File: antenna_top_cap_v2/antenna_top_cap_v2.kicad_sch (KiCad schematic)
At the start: 55 parts, among them IC1 PCT2075DP,118, J1 Battery Charge Bypass, J10 BM04B-SRSS-TB(LF)(SN), J12 BM04B-SRSS-TB(LF)(SN), J14 BM04B-SRSS-TB(LF)(SN), J16 BM04B-SRSS-TB(LF)(SN), J19 Z+_Cap_Connector, J2 EPS USB Bootselect Jumper, J3 EPS Reset Jumper, J4 BM04B-SRSS-TB(LF)(SN)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

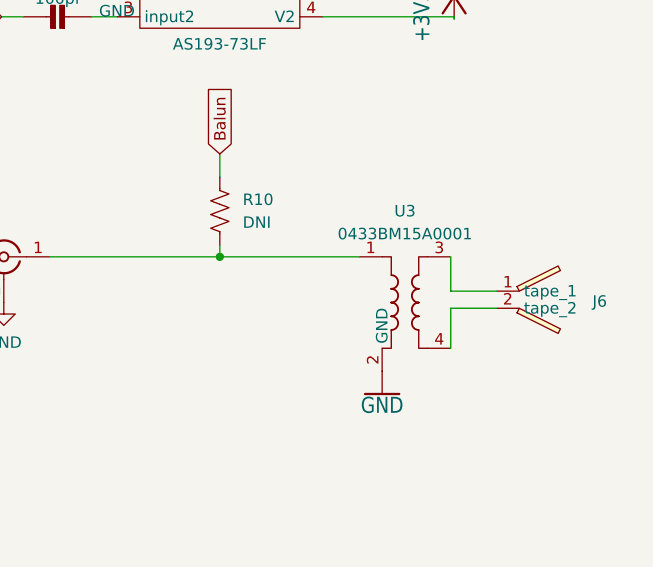
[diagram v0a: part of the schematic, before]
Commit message: Swapped Balun
New Balun Part Number!
Minicircuits: NCS1.5-232+

Schematic and PCB Layout Updated
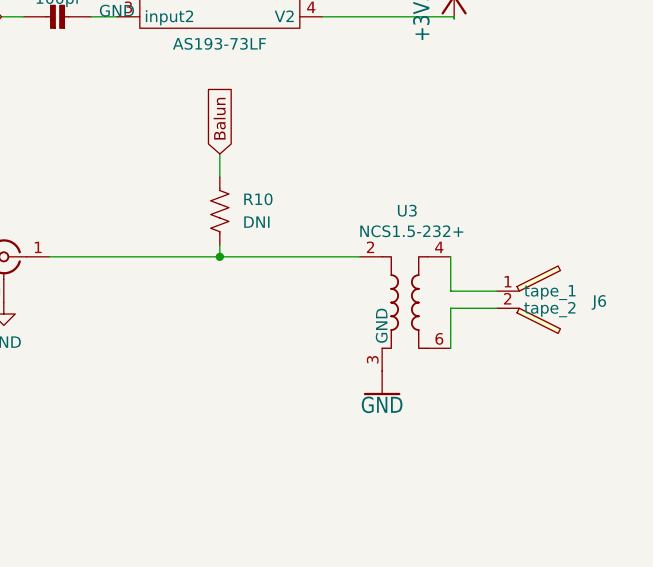
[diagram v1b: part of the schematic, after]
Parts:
- U3: value 0433BM15A0001 -> NCS1.5-232+
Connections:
- net GND: now also U3.1 (GND), U3.3 (GND); no longer U3.2 (GND), U3.5 (GND), U3.6 (GND)
- net at J6.1 (tape_1): now also U3.4; no longer U3.3
- net at J6.2 (tape_2): now also U3.6; no longer U3.4
- net at J6.1 (In), R10.2: now also U3.2; no longer U3.1

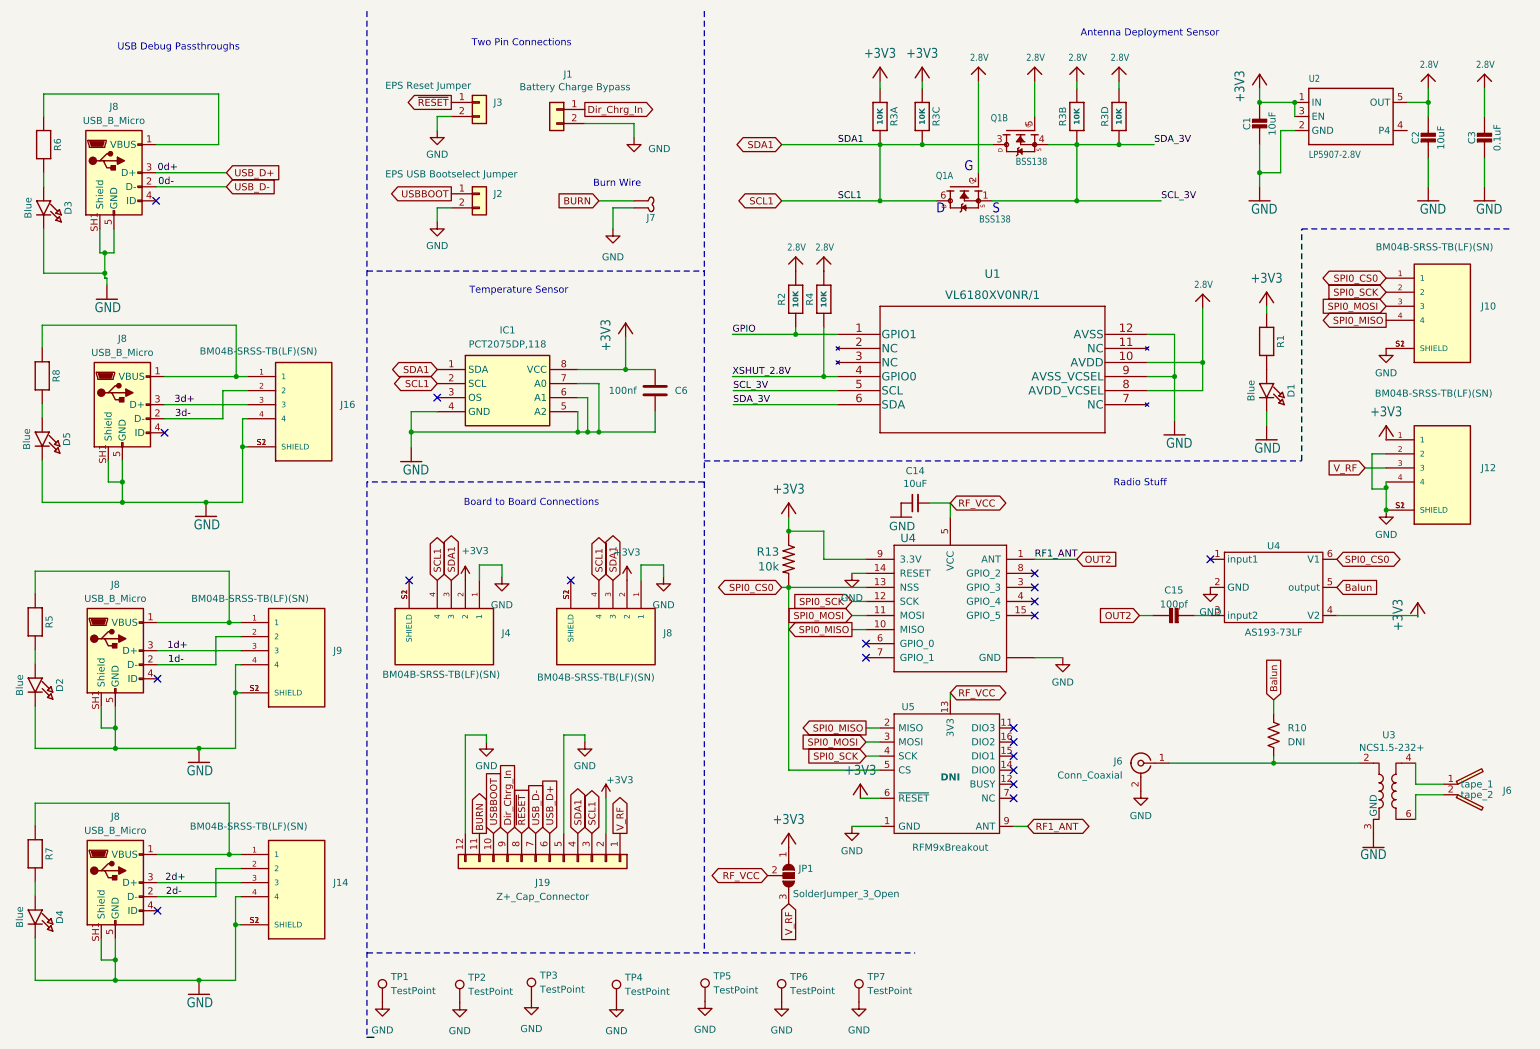
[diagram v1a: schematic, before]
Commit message: Added Schematic Symbols for FC Debug Port
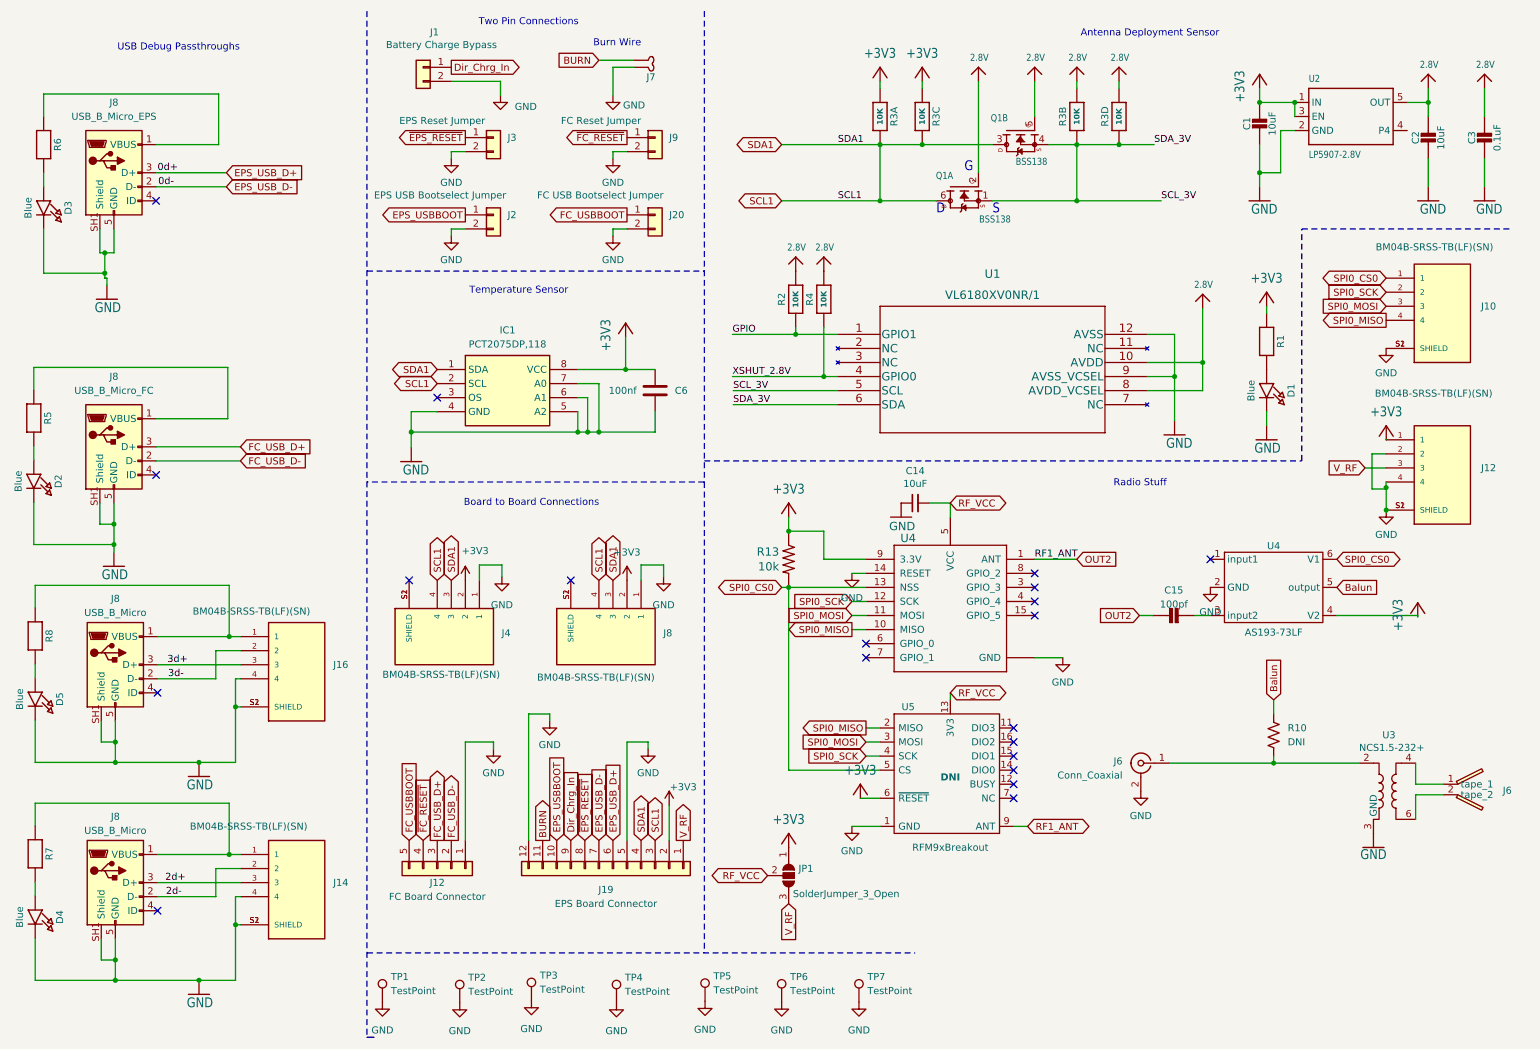
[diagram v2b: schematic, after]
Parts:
- removed J9: BM04B-SRSS-TB(LF)(SN), Antenna_board:JST_BM04B-SRSS-TB(LF)(SN), symbol BM04B-SRSS-TB_LF__SN_:BM04B-SRSS-TB(LF)(SN)
- added J12: FC Board Connector, FC_DEV_BOARD:MOLEX_5040500591, symbol Max_Lib:Connector_Generic_Conn_01x05
- added J20: FC USB Bootselect Jumper, Connector_PinHeader_2.54mm:PinHeader_1x02_P2.54mm_Vertical, symbol Connector_Generic:Conn_01x02
- added J9: FC Reset Jumper, Connector_PinHeader_2.54mm:PinHeader_1x02_P2.54mm_Vertical, symbol Connector_Generic:Conn_01x02
- J19: value Z+_Cap_Connector -> EPS Board Connector
- J8: value USB_B_Micro -> USB_B_Micro_EPS
- J8: value USB_B_Micro -> USB_B_Micro_FC
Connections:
- net GND: now also J12.1 (Pin_1), J20.2 (Pin_2), J9.2 (Pin_2)
- net 1d+ renamed FC_USB_D+
- net FC_USB_D+: now also J12.3 (Pin_3)
- net 1d- renamed FC_USB_D-
- net FC_USB_D-: now also J12.2 (Pin_2)
- net USBBOOT renamed EPS_USBBOOT
- net USB_D+ renamed EPS_USB_D+
- net USB_D- renamed EPS_USB_D-
- net ~{RESET} renamed ~{EPS_RESET}
- new net FC_USBBOOT: J12.5 (Pin_5), J20.1 (Pin_1)
- new net ~{FC_RESET}: J12.4 (Pin_4), J9.1 (Pin_1)
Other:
- moved on the sheet: D2, D5, J1, J16, J19, J2, J3, J7, J8, R5, R8

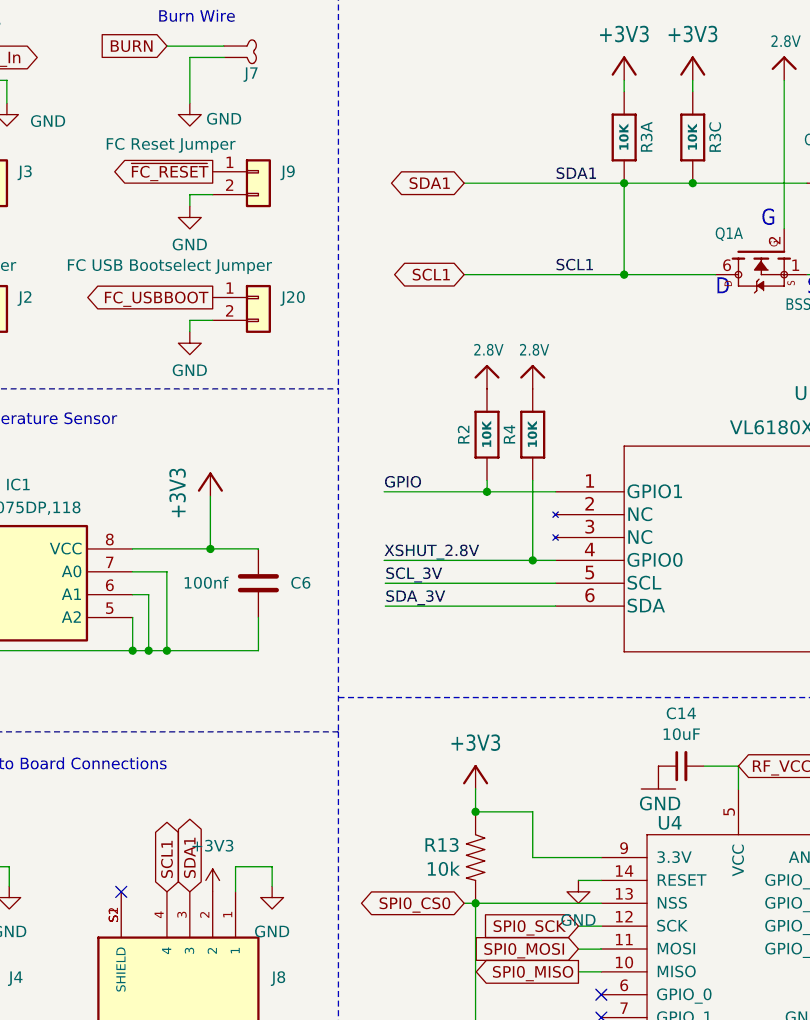
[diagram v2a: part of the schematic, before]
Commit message: SDA / SCL Hotfix
See this issue: https://github.com/proveskit/antenna-board/issues/6
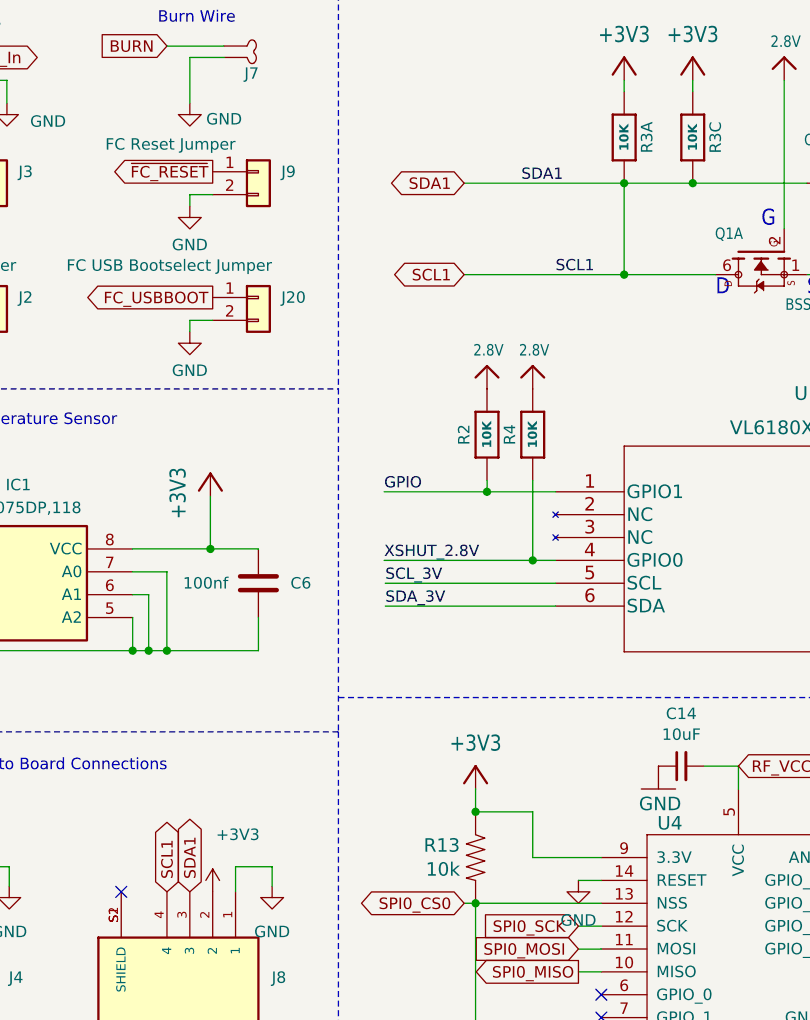
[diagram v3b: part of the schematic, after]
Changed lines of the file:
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@@
 	(wire
 		(pts
-			(xy 170.18 35.56) (xy 152.4 35.56)
-		)
-		(stroke
-			(width 0)
-			(type default)
-		)
-	)
-	(wire
-		(pts
 			(xy 228.473 74.93) (xy 228.473 65.151)
 		)
@@
 	(wire
 		(pts
+			(xy 152.4 35.56) (xy 170.18 35.56)
+		)
+		(stroke
+			(width 0)
+			(type default)
+		)
+	)
+	(wire
+		(pts
 			(xy 154.94 69.85) (xy 162.56 69.85)
 		)
@@
 	)
 	(label "SDA1"
-		(at 162.56 35.56 0)
+		(at 158.75 35.56 0)
 		(fields_autoplaced yes)
 		(effects
@@
 		(on_board yes)
 		(dnp no)
-		(fields_autoplaced yes)
 		(property "Reference" "#PWR053"
 			(at 124.46 118.11 0)
@@
 		)
 		(property "Value" "+3V3"
-			(at 124.46 109.22 0)
+			(at 127.254 107.95 0)
 			(effects
 				(font

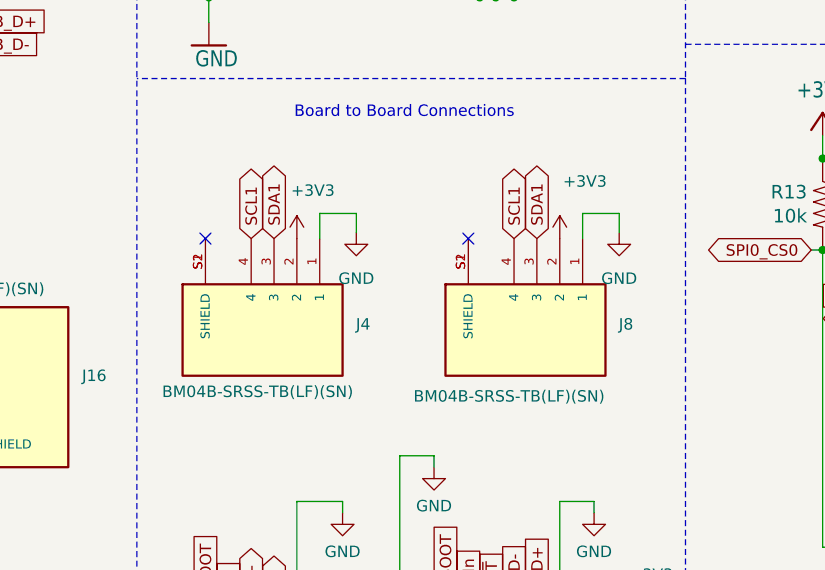
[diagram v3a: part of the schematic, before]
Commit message: Removed J8 (I2C Breakout)
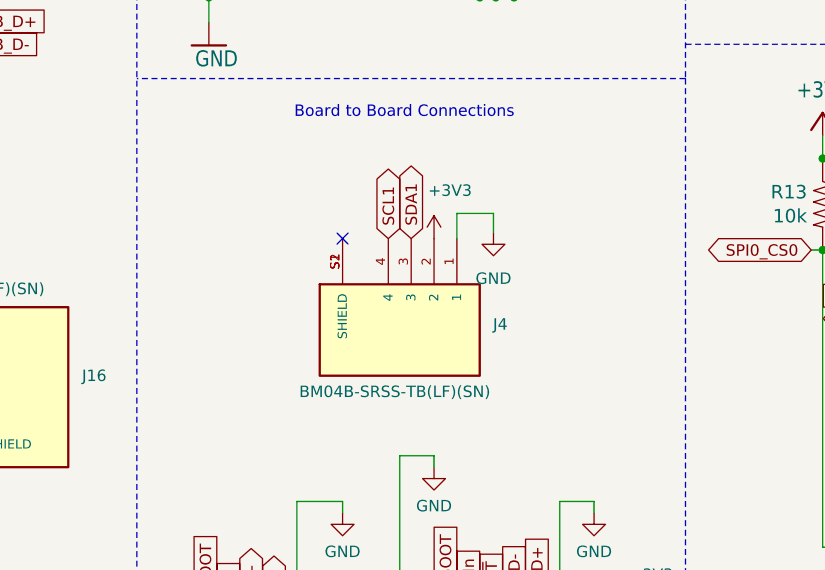
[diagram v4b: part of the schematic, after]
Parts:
- removed J8: BM04B-SRSS-TB(LF)(SN), Antenna_board:JST_BM04B-SRSS-TB(LF)(SN), symbol BM04B-SRSS-TB_LF__SN_:BM04B-SRSS-TB(LF)(SN)
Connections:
- no-connect marks 20 -> 19
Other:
- moved on the sheet: J4

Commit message: fixed the schematic
cool beans
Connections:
- net SCL1: no longer IC1.1 (SDA), J19.4 (Pin_4), J4.3, Q1.3 (D), R3.6 (2)
- net SCL_3V: no longer Q1.4 (S), R3.5 (2), U1.6 (SDA)
- new net SDA1: IC1.1 (SDA), J19.4 (Pin_4), J4.3, Q1.3 (D), R3.6 (2)
- new net SDA_3V: Q1.4 (S), R3.5 (2), U1.6 (SDA)
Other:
- moved on the sheet: R3A, R3B
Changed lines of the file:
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@@
 	)
 	(junction
-		(at 205.74 35.56)
-		(diameter 0)
-		(color 0 0 0 0)
-	)
-	(junction
 		(at 223.393 77.47)
 		(diameter 0)
@@
 	)
 	(junction
-		(at 170.18 35.56)
-		(diameter 0)
-		(color 0 0 0 0)
-	)
-	(junction
 		(at 32.004 147.193)
 		(diameter 0)
@@
 	(wire
 		(pts
-			(xy 205.74 35.56) (xy 205.74 45.72)
+			(xy 205.74 36.83) (xy 205.74 45.72)
 		)
 		(stroke
@@
 	(wire
 		(pts
-			(xy 152.4 35.56) (xy 170.18 35.56)
-		)
-		(stroke
-			(width 0)
-			(type default)
-		)
-	)
-	(wire
-		(pts
 			(xy 154.94 69.85) (xy 162.56 69.85)
 		)
@@
 	(wire
 		(pts
-			(xy 205.74 25.4) (xy 205.74 24.13)
+			(xy 205.74 26.67) (xy 205.74 24.13)
 		)
 		(stroke
@@
 	(wire
 		(pts
-			(xy 177.8 35.56) (xy 170.18 35.56)
+			(xy 152.4 35.56) (xy 177.8 35.56)
 		)
 		(stroke
@@
 	(wire
 		(pts
-			(xy 170.18 24.13) (xy 170.18 25.4)
+			(xy 170.18 24.13) (xy 170.18 26.67)
 		)
 		(stroke
@@
 	(wire
 		(pts
-			(xy 200.66 35.56) (xy 205.74 35.56)
+			(xy 200.66 35.56) (xy 213.36 35.56)
 		)
 		(stroke
@@
 	(wire
 		(pts
-			(xy 205.74 35.56) (xy 213.36 35.56)
-		)
-		(stroke
-			(width 0)
-			(type default)
-		)
-	)
-	(wire
-		(pts
 			(xy 167.64 123.19) (xy 165.1 123.19)
 		)
@@
 	(wire
 		(pts
-			(xy 170.18 35.56) (xy 170.18 45.72)
+			(xy 170.18 36.83) (xy 170.18 45.72)
 		)
 		(stroke
@@
 	(symbol
 		(lib_id "Adafruit VL6180 Time of Flight Sensor-eagle-import:RESISTOR_4PACK")
-		(at 205.74 30.48 90)
+		(at 205.74 31.75 90)
 		(mirror x)
 		(unit 2)
@@
 		(dnp no)
 		(property "Reference" "R3"
-			(at 203.2 30.48 0)
+			(at 203.2 31.75 0)
 			(effects
 				(font
@@
 		)
 		(property "Value" "10K"
-			(at 205.74 30.48 0)
+			(at 205.74 31.75 0)
 			(effects
 				(font
@@
 		)
 		(property "Footprint" "Resistor_SMD:R_Array_Convex_4x0603"
-			(at 205.74 30.48 0)
+			(at 205.74 31.75 0)
 			(effects
 				(font
@@
 		)
 		(property "Datasheet" ""
-			(at 205.74 30.48 0)
+			(at 205.74 31.75 0)
 			(effects
 				(font
@@
 		)
 		(property "Description" ""
-			(at 205.74 30.48 0)
+			(at 205.74 31.75 0)
 			(effects
 				(font
@@
 	(symbol
 		(lib_id "Adafruit VL6180 Time of Flight Sensor-eagle-import:RESISTOR_4PACK")
-		(at 170.18 30.48 270)
+		(at 170.18 31.75 270)
 		(unit 1)
 		(exclude_from_sim no)
@@
 		(dnp no)
 		(property "Reference" "R3"
-			(at 172.72 30.48 0)
+			(at 172.72 31.75 0)
 			(effects
 				(font
@@
 		)
 		(property "Value" "10K"
-			(at 170.18 30.48 0)
+			(at 170.18 31.75 0)
 			(effects
 				(font
@@
 		)
 		(property "Footprint" "Resistor_SMD:R_Array_Convex_4x0603"
-			(at 170.18 30.48 0)
+			(at 170.18 31.75 0)
 			(effects
 				(font
@@
 		)
 		(property "Datasheet" ""
-			(at 170.18 30.48 0)
+			(at 170.18 31.75 0)
 			(effects
 				(font
@@
 		)
 		(property "Description" ""
-			(at 170.18 30.48 0)
+			(at 170.18 31.75 0)
 			(effects
 				(font

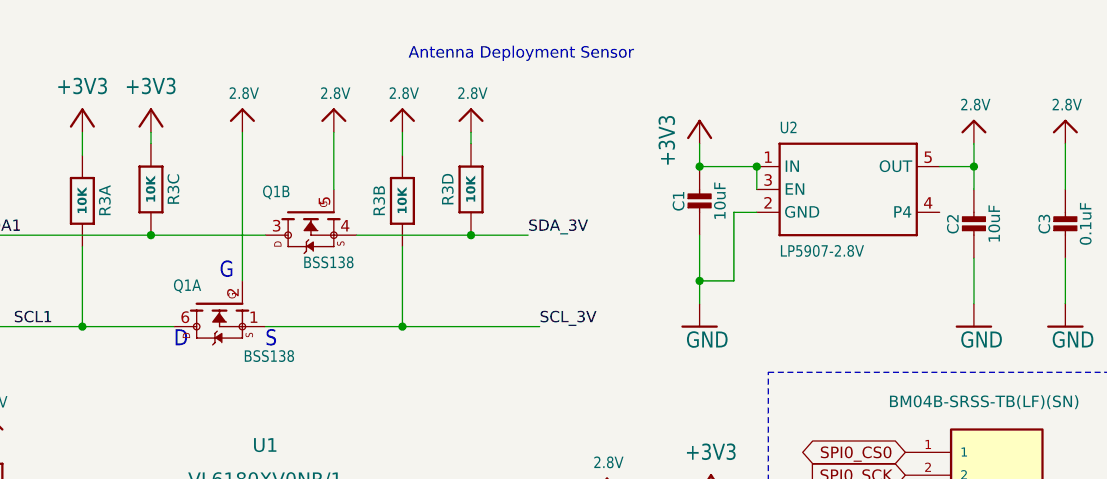
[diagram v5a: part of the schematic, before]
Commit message: Completed LiDAR Layout
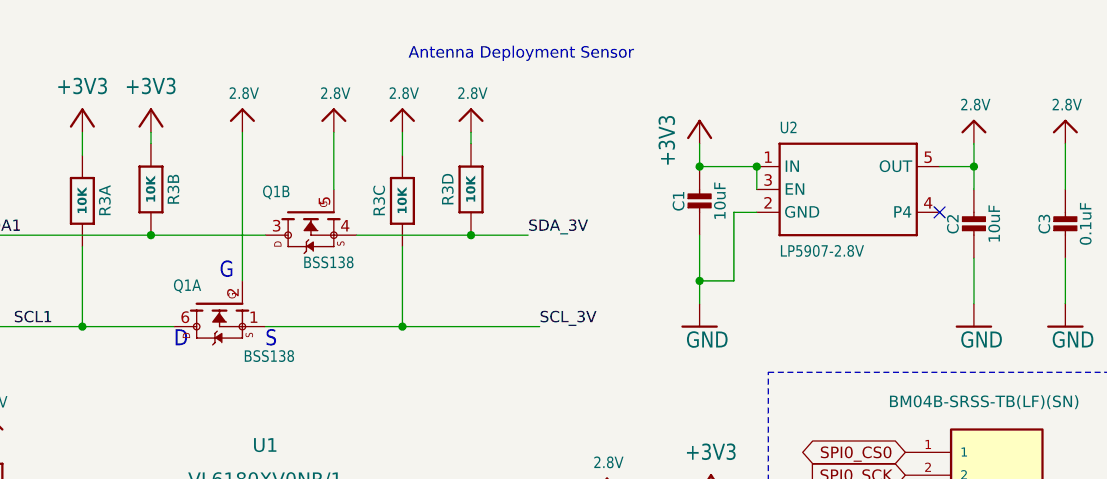
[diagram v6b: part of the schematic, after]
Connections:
- net +3V3: now also R3.2 (1); no longer R3.3 (1)
- net 2.8V: now also R3.3 (1); no longer R3.2 (1)
- net SCL_3V: now also R3.6 (2); no longer R3.7 (2)
- net SDA1: now also R3.7 (2); no longer R3.6 (2)
- no-connect marks 19 -> 20
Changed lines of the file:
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@@
 	)
 	(no_connect
+		(at 265.43 33.02)
+	)
+	(no_connect
 		(at 167.64 128.27)
 	)
@@
 		(at 205.74 31.75 90)
 		(mirror x)
-		(unit 2)
+		(unit 3)
 		(exclude_from_sim no)
 		(in_bom yes)
@@
 				(path "/e63e39d7-6ac0-4ffd-8aa3-1841a4541b55"
 					(reference "R3")
-					(unit 2)
+					(unit 3)
 				)
 			)
@@
 		(lib_id "Adafruit VL6180 Time of Flight Sensor-eagle-import:RESISTOR_4PACK")
 		(at 177.8 30.48 270)
-		(unit 3)
+		(unit 2)
 		(exclude_from_sim no)
 		(in_bom yes)
@@
 				(path "/e63e39d7-6ac0-4ffd-8aa3-1841a4541b55"
 					(reference "R3")
-					(unit 3)
+					(unit 2)
 				)
 			)
